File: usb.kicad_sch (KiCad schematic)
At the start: 80 parts, among them J1 USB_C_Receptacle_USB2.0, J2 USB_C_Receptacle_USB2.0, J3 USB_C_Receptacle_USB2.0, J4 USB_C_Receptacle_USB2.0, U1 MIMX8MM6DVTLZAA, U10 D5V0H1B2LP, U11 TPD4EUSB30, U12 TPD4EUSB30, U13 74LVC2G07, U14 D5V0H1B2LP, U15 CH343P, U16 TPD4EUSB30, U17 INA231, U18 D5V0H1B2LP, U19 TS3USB221E, U20 TPD4EUSB30, U4 74LVC2G04, U5 NX5P3363, U6 TUSB320LAI, U7 NX5P3363, U8 TUSB320LAI, U9 D5V0H1B2LP

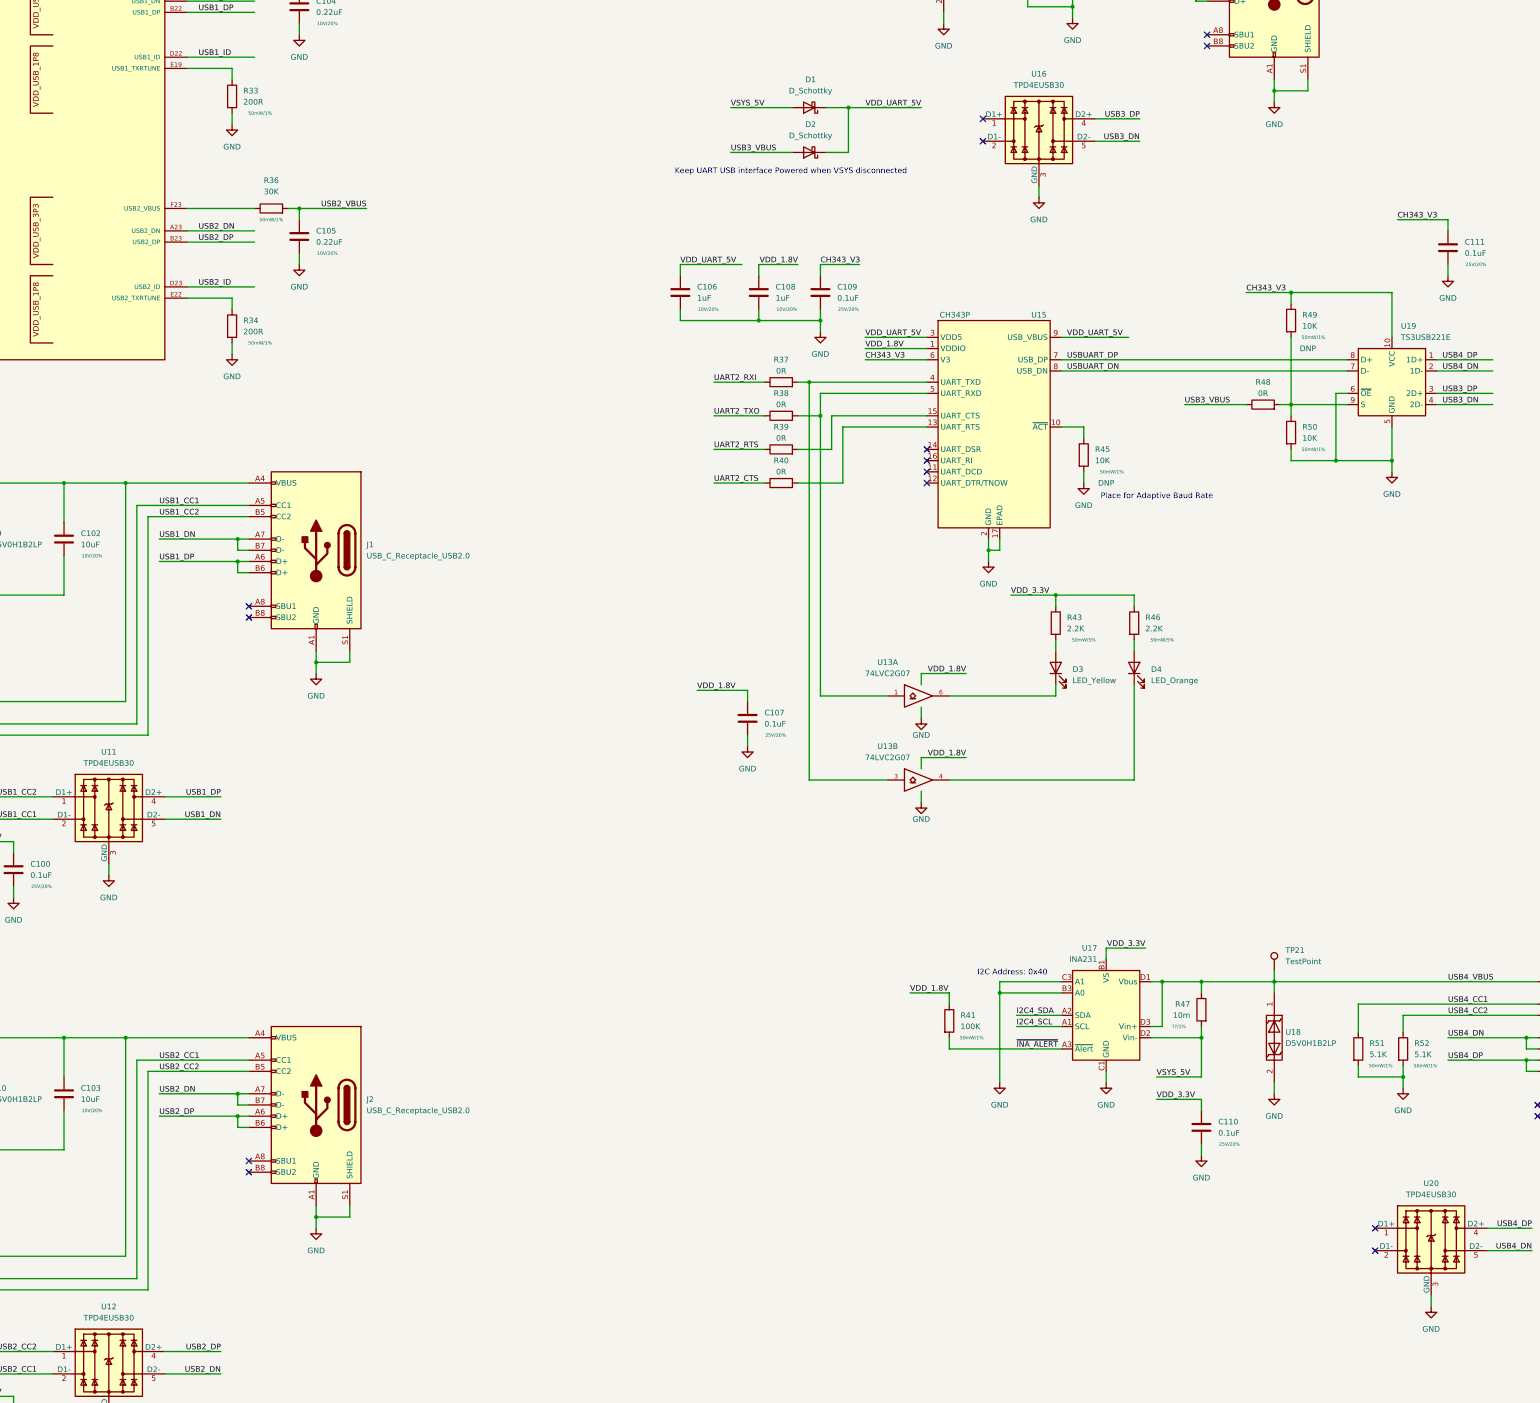
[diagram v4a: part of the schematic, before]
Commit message: add SN65DSI86 DSI2DP ic, SCH, PCB work, flytime work
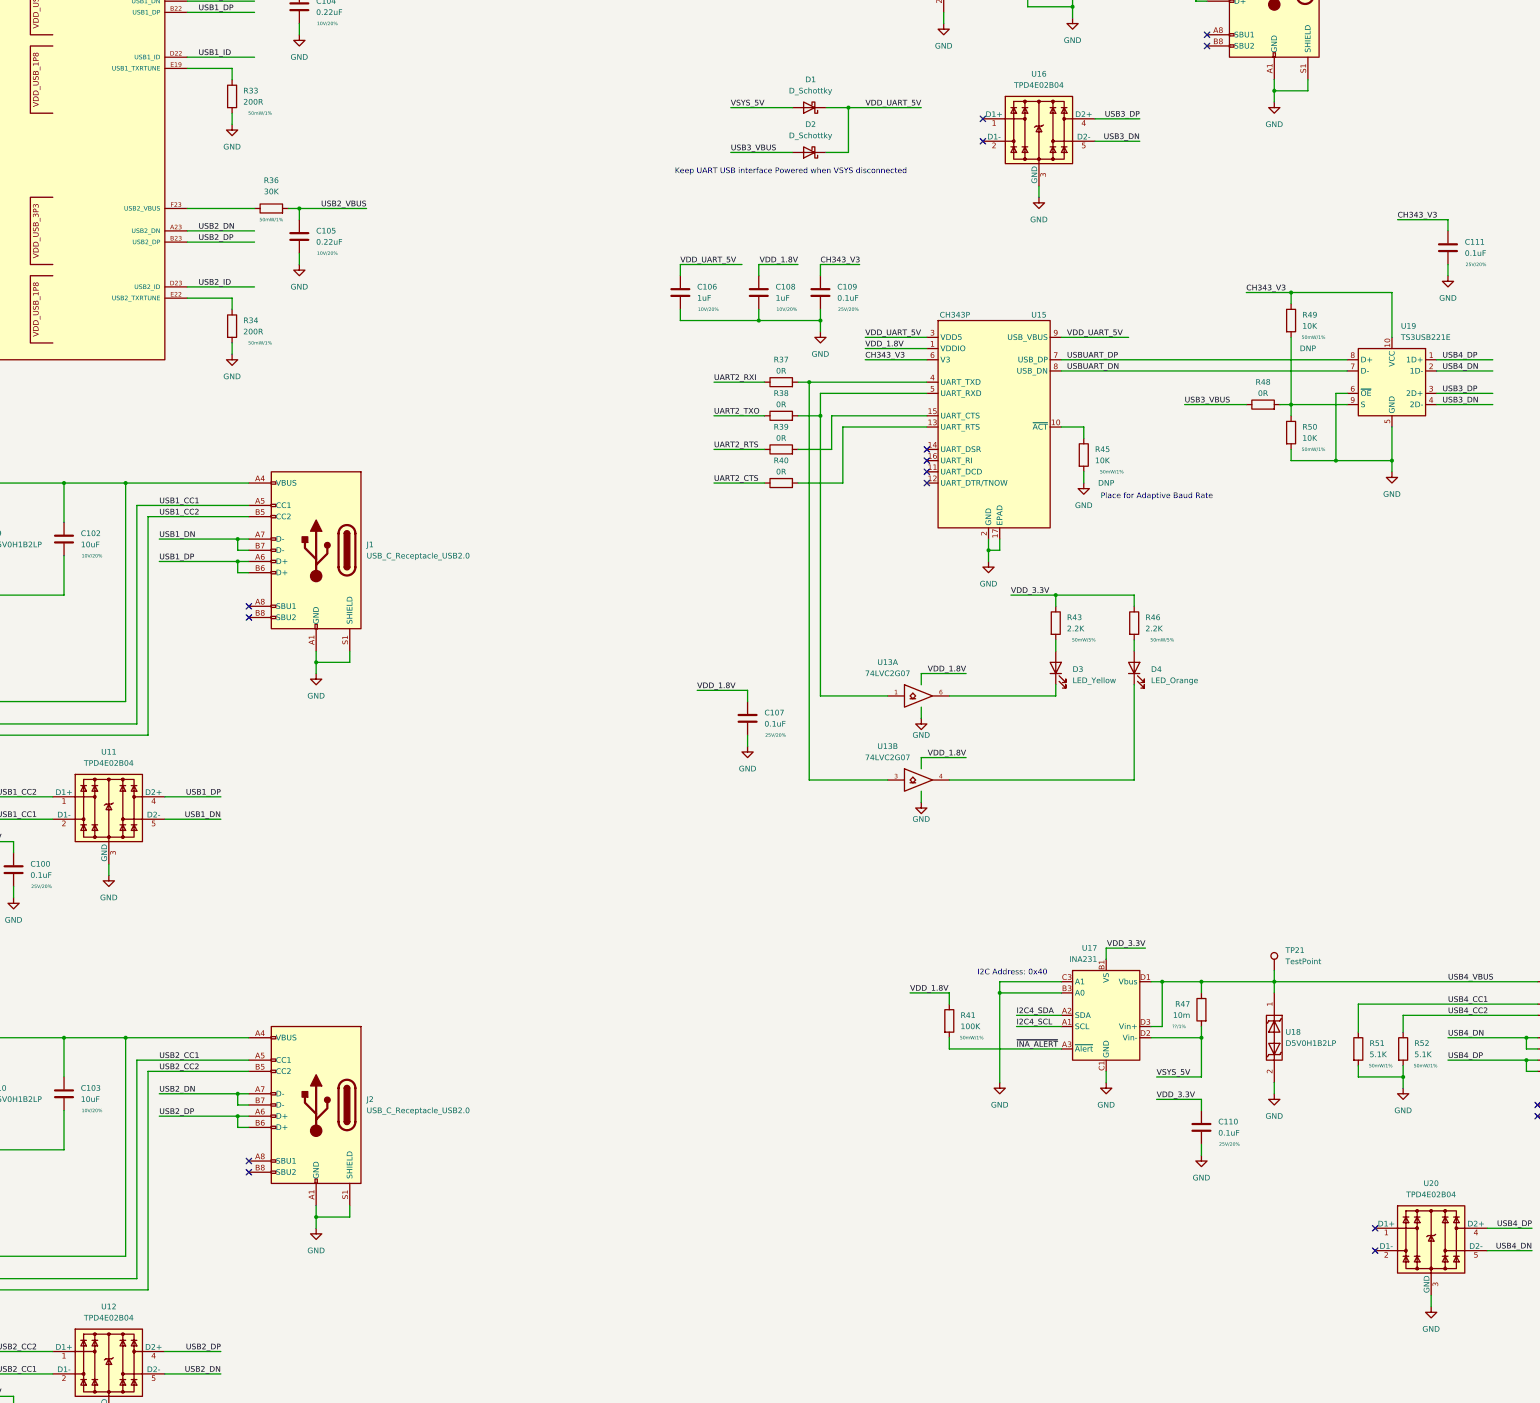
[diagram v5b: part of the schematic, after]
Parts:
- removed U11, U12, U16, U20: TPD4EUSB30, Package_SON:USON-10_2.5x1.0mm_P0.5mm, symbol qsbc:TPD4EUSB30
- added U11, U12, U16, U20: TPD4E02B04, Package_SON:USON-10_2.5x1.0mm_P0.5mm, symbol qsbc:TPD4E02B04
- J3: footprint Connector_USB:USB_C_Receptacle_HRO_TYPE-C-31-M-12 -> qsbc:12402054M611A
- R34: footprint Resistor_SMD:R_0402_1005Metric -> qsbc:R_0201_0603Metric
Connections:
- net GND: now also U11.3 (GND), U11.8 (GND), U12.3 (GND), U12.8 (GND), U16.3 (GND), U16.8 (GND), U20.3 (GND), U20.8 (GND)
- net USB1_CC1: now also U11.2 (D1-), U11.9
- net USB1_CC2: now also U11.1 (D1+), U11.10
- net USB1_DN: now also U11.5 (D2-), U11.6
- net USB1_DP: now also U11.4 (D2+), U11.7
- net USB2_CC1: now also U12.2 (D1-), U12.9
- net USB2_CC2: now also U12.1 (D1+), U12.10
- net USB2_DN: now also U12.5 (D2-), U12.6
- net USB2_DP: now also U12.4 (D2+), U12.7
- net USB3_DN: now also U16.5 (D2-), U16.6
- net USB3_DP: now also U16.4 (D2+), U16.7
- net USB4_DN: now also U20.5 (D2-), U20.6
- net USB4_DP: now also U20.4 (D2+), U20.7
- new net: U20.1 (D1+), U20.10
- new net: U20.2 (D1-), U20.9
- new net: U16.1 (D1+), U16.10
- new net: U16.2 (D1-), U16.9
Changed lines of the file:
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@@
     (stroke (width 0) (type default) (color 0 0 0 0))
   )
-  (wire (pts (xy 469.9 340.36) (xy 480.06 340.36))
+  (wire (pts (xy 469.9 335.28) (xy 480.06 335.28))
     (stroke (width 0) (type default) (color 0 0 0 0))
   )
@@
     (stroke (width 0) (type default) (color 0 0 0 0))
   )
-  (wire (pts (xy 469.9 335.28) (xy 480.06 335.28))
+  (wire (pts (xy 469.9 340.36) (xy 480.06 340.36))
     (stroke (width 0) (type default) (color 0 0 0 0))
   )
@@
     (pin "2")
   )
+  (symbol (lib_id "qsbc:TPD4E02B04") (at 457.2 337.82 0) (unit 1)
+    (in_bom yes) (on_board yes) (fields_autoplaced)
+    (property "Reference" "U20" (id 0) (at 457.2 325.12 0))
+    (property "Value" "TPD4E02B04" (id 1) (at 457.2 327.66 0))
+    (property "Footprint" "Package_SON:USON-10_2.5x1.0mm_P0.5mm" (id 2) (at 433.07 347.98 0)
+      (effects (font (size 1.27 1.27)) hide)
+    )
+    (property "Datasheet" "https://www.ti.com/lit/ds/symlink/tpd4e02b04.pdf" (id 3) (at 457.2 337.82 0)
+      (effects (font (size 1.27 1.27)) hide)
+    )
+    (pin "1")
+    (pin "10")
+    (pin "2")
+    (pin "3")
+    (pin "4")
+    (pin "5")
+    (pin "6")
+    (pin "7")
+    (pin "8")
+    (pin "9")
+  )
   (symbol (lib_id "Device:D_Schottky") (at 316.23 91.44 180) (unit 1)
     (in_bom yes) (on_board yes) (fields_autoplaced)
@@
     (pin "9")
   )
-  (symbol (lib_id "qsbc:TPD4EUSB30") (at 157.48 240.03 0) (unit 1)
+  (symbol (lib_id "qsbc:TPD4E02B04") (at 368.3 86.36 0) (unit 1)
     (in_bom yes) (on_board yes) (fields_autoplaced)
-    (property "Reference" "U11" (id 0) (at 157.48 227.33 0))
-    (property "Value" "TPD4EUSB30" (id 1) (at 157.48 229.87 0))
-    (property "Footprint" "Package_SON:USON-10_2.5x1.0mm_P0.5mm" (id 2) (at 133.35 250.19 0)
+    (property "Reference" "U16" (id 0) (at 368.3 73.66 0))
+    (property "Value" "TPD4E02B04" (id 1) (at 368.3 76.2 0))
+    (property "Footprint" "Package_SON:USON-10_2.5x1.0mm_P0.5mm" (id 2) (at 344.17 96.52 0)
       (effects (font (size 1.27 1.27)) hide)
     )
-    (property "Datasheet" "http://www.ti.com/lit/ds/symlink/tpd2eusb30a.pdf" (id 3) (at 157.48 240.03 0)
+    (property "Datasheet" "https://www.ti.com/lit/ds/symlink/tpd4e02b04.pdf" (id 3) (at 368.3 86.36 0)
       (effects (font (size 1.27 1.27)) hide)
     )
@@
     (pin "2")
   )
-  (symbol (lib_id "qsbc:TPD4EUSB30") (at 368.3 86.36 0) (unit 1)
-    (in_bom yes) (on_board yes) (fields_autoplaced)
-    (property "Reference" "U16" (id 0) (at 368.3 73.66 0))
-    (property "Value" "TPD4EUSB30" (id 1) (at 368.3 76.2 0))
-    (property "Footprint" "Package_SON:USON-10_2.5x1.0mm_P0.5mm" (id 2) (at 344.17 96.52 0)
-      (effects (font (size 1.27 1.27)) hide)
-    )
-    (property "Datasheet" "http://www.ti.com/lit/ds/symlink/tpd2eusb30a.pdf" (id 3) (at 368.3 86.36 0)
-      (effects (font (size 1.27 1.27)) hide)
-    )
-    (pin "1")
-    (pin "10")
-    (pin "2")
-    (pin "3")
-    (pin "4")
-    (pin "5")
-    (pin "6")
-    (pin "7")
-    (pin "8")
-    (pin "9")
-  )
   (symbol (lib_id "power:GND") (at 356.87 184.15 0) (unit 1)
     (in_bom yes) (on_board yes) (fields_autoplaced)
@@
     (pin "2")
   )
-  (symbol (lib_id "qsbc:TPD4EUSB30") (at 157.48 365.76 0) (unit 1)
-    (in_bom yes) (on_board yes) (fields_autoplaced)
-    (property "Reference" "U12" (id 0) (at 157.48 353.06 0))
-    (property "Value" "TPD4EUSB30" (id 1) (at 157.48 355.6 0))
-    (property "Footprint" "Package_SON:USON-10_2.5x1.0mm_P0.5mm" (id 2) (at 133.35 375.92 0)
-      (effects (font (size 1.27 1.27)) hide)
-    )
-    (property "Datasheet" "http://www.ti.com/lit/ds/symlink/tpd2eusb30a.pdf" (id 3) (at 157.48 365.76 0)
-      (effects (font (size 1.27 1.27)) hide)
-    )
-    (pin "1")
-    (pin "10")
-    (pin "2")
-    (pin "3")
-    (pin "4")
-    (pin "5")
-    (pin "6")
-    (pin "7")
-    (pin "8")
-    (pin "9")
-  )
   (symbol (lib_id "Device:R") (at 48.26 322.58 0) (unit 1)
     (in_bom yes) (on_board yes)
@@
     (pin "2")
   )
+  (symbol (lib_id "qsbc:TPD4E02B04") (at 157.48 365.76 0) (unit 1)
+    (in_bom yes) (on_board yes) (fields_autoplaced)
+    (property "Reference" "U12" (id 0) (at 157.48 353.06 0))
+    (property "Value" "TPD4E02B04" (id 1) (at 157.48 355.6 0))
+    (property "Footprint" "Package_SON:USON-10_2.5x1.0mm_P0.5mm" (id 2) (at 133.35 375.92 0)
+      (effects (font (size 1.27 1.27)) hide)
+    )
+    (property "Datasheet" "https://www.ti.com/lit/ds/symlink/tpd4e02b04.pdf" (id 3) (at 157.48 365.76 0)
+      (effects (font (size 1.27 1.27)) hide)
+    )
+    (pin "1")
+    (pin "10")
+    (pin "2")
+    (pin "3")
+    (pin "4")
+    (pin "5")
+    (pin "6")
+    (pin "7")
+    (pin "8")
+    (pin "9")
+  )
   (symbol (lib_id "Connector:USB_C_Receptacle_USB2.0") (at 421.64 52.07 0) (mirror y) (unit 1)
     (in_bom yes) (on_board yes) (fields_autoplaced)
@@
       (effects (font (size 1.27 1.27)) (justify right))
     )
-    (property "Footprint" "Connector_USB:USB_C_Receptacle_HRO_TYPE-C-31-M-12" (id 2) (at 417.83 52.07 0)
+    (property "Footprint" "qsbc:12402054M611A" (id 2) (at 417.83 52.07 0)
       (effects (font (size 1.27 1.27)) hide)
     )
@@
     (pin "2")
   )
+  (symbol (lib_id "qsbc:TPD4E02B04") (at 157.48 240.03 0) (unit 1)
+    (in_bom yes) (on_board yes) (fields_autoplaced)
+    (property "Reference" "U11" (id 0) (at 157.48 227.33 0))
+    (property "Value" "TPD4E02B04" (id 1) (at 157.48 229.87 0))
+    (property "Footprint" "Package_SON:USON-10_2.5x1.0mm_P0.5mm" (id 2) (at 133.35 250.19 0)
+      (effects (font (size 1.27 1.27)) hide)
+    )
+    (property "Datasheet" "https://www.ti.com/lit/ds/symlink/tpd4e02b04.pdf" (id 3) (at 157.48 240.03 0)
+      (effects (font (size 1.27 1.27)) hide)
+    )
+    (pin "1")
+    (pin "10")
+    (pin "2")
+    (pin "3")
+    (pin "4")
+    (pin "5")
+    (pin "6")
+    (pin "7")
+    (pin "8")
+    (pin "9")
+  )
   (symbol (lib_id "Device:R") (at 375.92 52.07 0) (unit 1)
     (in_bom yes) (on_board yes)
@@
       (effects (font (size 1.27 1.27)) (justify left))
     )
-    (property "Footprint" "Resistor_SMD:R_0402_1005Metric" (id 2) (at 183.642 130.81 90)
+    (property "Footprint" "qsbc:R_0201_0603Metric" (id 2) (at 183.642 130.81 90)
       (effects (font (size 1.27 1.27)) hide)
     )
@@
     (pin "1")
   )
-  (symbol (lib_id "qsbc:TPD4EUSB30") (at 457.2 337.82 0) (unit 1)
-    (in_bom yes) (on_board yes) (fields_autoplaced)
-    (property "Reference" "U20" (id 0) (at 457.2 325.12 0))
-    (property "Value" "TPD4EUSB30" (id 1) (at 457.2 327.66 0))
-    (property "Footprint" "Package_SON:USON-10_2.5x1.0mm_P0.5mm" (id 2) (at 433.07 347.98 0)
-      (effects (font (size 1.27 1.27)) hide)
-    )
-    (property "Datasheet" "http://www.ti.com/lit/ds/symlink/tpd2eusb30a.pdf" (id 3) (at 457.2 337.82 0)
-      (effects (font (size 1.27 1.27)) hide)
-    )
-    (pin "1")
-    (pin "10")
-    (pin "2")
-    (pin "3")
-    (pin "4")
-    (pin "5")
-    (pin "6")
-    (pin "7")
-    (pin "8")
-    (pin "9")
-  )
   (symbol (lib_id "qsbc:D5V0H1B2LP") (at 129.54 179.07 270) (unit 1)
